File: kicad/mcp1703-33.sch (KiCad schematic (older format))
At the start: 3 parts, among them U3 MCP1703A-3302_SOT23

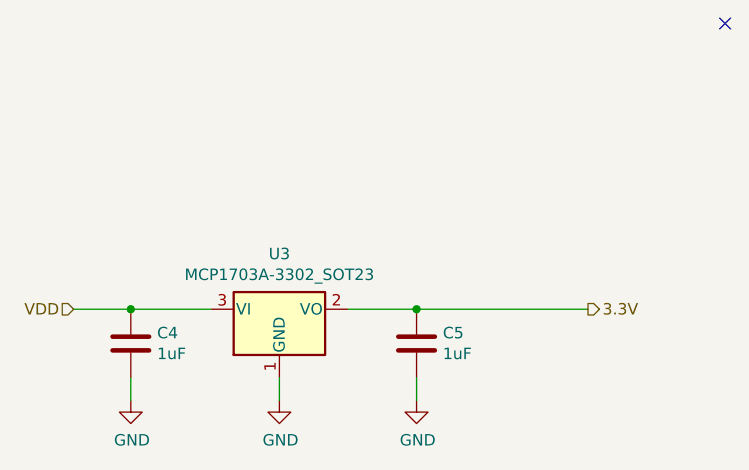
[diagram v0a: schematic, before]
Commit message: add more test points
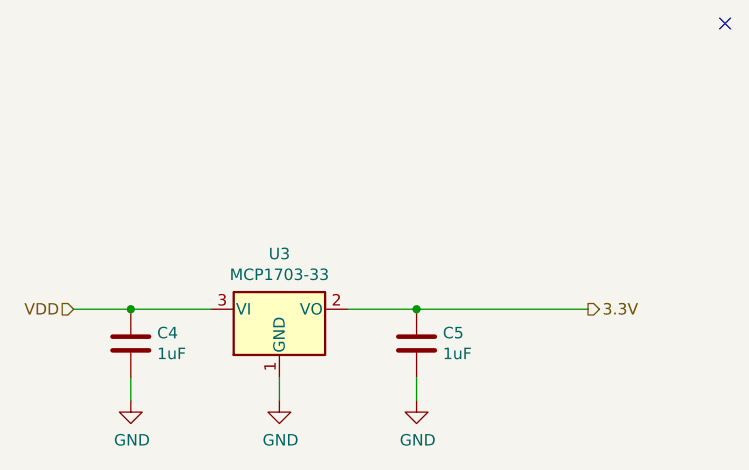
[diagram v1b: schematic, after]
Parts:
- U3: value MCP1703A-3302_SOT23 -> MCP1703-33
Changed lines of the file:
@@
 P 5300 4000
 F 0 "U3" H 5300 4242 50  0000 C CNN
-F 1 "MCP1703A-3302_SOT23" H 5300 4151 50  0000 C CNN
+F 1 "MCP1703-33" H 5300 4151 50  0000 C CNN
 F 2 "Package_TO_SOT_SMD:SOT-23" H 5300 4200 50  0001 C CNN
 F 3 "http://ww1.microchip.com/downloads/en/DeviceDoc/20005122B.pdf" H 5300 3950 50  0001 C CNN
